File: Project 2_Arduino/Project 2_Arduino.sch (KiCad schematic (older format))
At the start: 30 parts, among them J10 Conn_01x08, J11 Conn_01x08, J12 Conn_01x06, J13 Conn_01x03, J3 USB_microB_2040002-1, J4 Conn_02x03_Odd_Even, SW1 SW_Push, U1 FT232RL, U3 ATMEGA328P-AU, Y1 16MHz

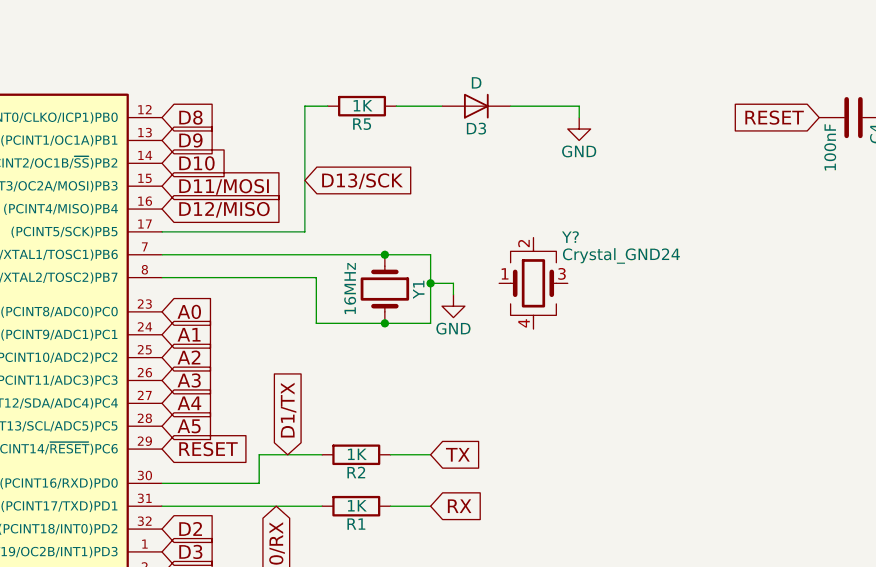
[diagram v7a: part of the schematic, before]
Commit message: new clock schematic
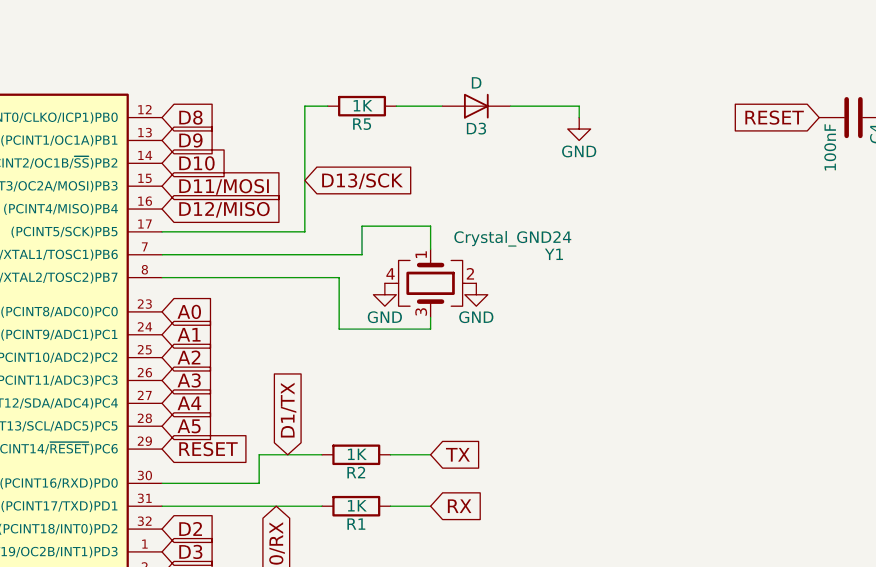
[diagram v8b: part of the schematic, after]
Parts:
- removed Y1: 16MHz, project2:TM16, symbol Crystal
- gave numbers to parts that had none: 1
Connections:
- net GND: now also Y1.2, Y1.4; no longer U3.7 ((PCINT6/XTAL1/TOSC1)PB6), U3.8 ((PCINT7/XTAL2/TOSC2)PB7)
- net at Y1.1: now also U3.7 ((PCINT6/XTAL1/TOSC1)PB6)
- net at Y1.3: now also U3.8 ((PCINT7/XTAL2/TOSC2)PB7)
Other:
- moved on the sheet: Y1
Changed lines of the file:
@@
 Text Notes 2275 1100 0    197  ~ 0
 Microcontroller
-$Comp
-L Crystal Y1
-U 1 1 59DFEE18
-P 5075 2400
-F 0 "Y1" H 5075 2550 50  0000 C CNN
-F 1 "16MHz" H 5075 2250 50  0000 C CNN
-F 2 "project2:TM16" H 5075 2400 50  0001 C CNN
-F 3 "" H 5075 2400 50  0001 C CNN
-	1    5075 2400
-	0    1    1    0
-$EndComp
 Wire Wire Line
 	2100 3950 2200 3950
@@
 Wire Wire Line
 	1200 5925 1150 5925
-Wire Wire Line
-	4100 2250 5275 2250
-Wire Wire Line
-	4100 2350 4775 2350
-Wire Wire Line
-	4775 2350 4775 2550
-Wire Wire Line
-	4775 2550 5275 2550
-Wire Wire Line
-	5275 2550 5275 2250
-Connection ~ 5075 2550
-Connection ~ 5075 2250
-Wire Wire Line
-	5275 2375 5375 2375
-Wire Wire Line
-	5375 2375 5375 2425
-Connection ~ 5275 2375
-$Comp
-L GND #PWR09
-U 1 1 59DFF36B
-P 5375 2425
-F 0 "#PWR09" H 5375 2175 50  0001 C CNN
-F 1 "GND" H 5375 2275 50  0000 C CNN
-F 2 "" H 5375 2425 50  0001 C CNN
-F 3 "" H 5375 2425 50  0001 C CNN
-	1    5375 2425
-	1    0    0    -1
-$EndComp
 Text Notes 8175 4825 0    197  ~ 0
 Header Pins
@@
 GND
 $Comp
-L Crystal_GND24 Y?
+L Crystal_GND24 Y1
 U 1 1 59DF0F95
-P 5725 2375
-F 0 "Y?" H 5850 2575 50  0000 L CNN
-F 1 "Crystal_GND24" H 5850 2500 50  0000 L CNN
-F 2 "" H 5725 2375 50  0001 C CNN
-F 3 "" H 5725 2375 50  0001 C CNN
-	1    5725 2375
-	1    0    0    -1
-$EndComp
+P 5275 2375
+F 0 "Y1" V 5150 2875 50  0000 L CNN
+F 1 "Crystal_GND24" V 5075 2475 50  0000 L CNN
+F 2 "" H 5275 2375 50  0001 C CNN
+F 3 "" H 5275 2375 50  0001 C CNN
+	1    5275 2375
+	0    1    1    0
+$EndComp
+Wire Wire Line
+	4100 2250 4975 2250
+Wire Wire Line
+	4975 2250 4975 2125
+Wire Wire Line
+	4975 2125 5275 2125
+Wire Wire Line
+	5275 2125 5275 2225
+Wire Wire Line
+	5275 2525 5275 2575
+Wire Wire Line
+	4875 2575 5275 2575
+Wire Wire Line
+	4875 2350 4875 2575
+Wire Wire Line
+	4875 2350 4100 2350
+$Comp
+L GND #PWR?
+U 1 1 59E16207
+P 5475 2375
+F 0 "#PWR?" H 5475 2125 50  0001 C CNN
+F 1 "GND" H 5475 2225 50  0000 C CNN
+F 2 "" H 5475 2375 50  0001 C CNN
+F 3 "" H 5475 2375 50  0001 C CNN
+	1    5475 2375
+	1    0    0    -1
+$EndComp
+$Comp
+L GND #PWR?
+U 1 1 59E16269
+P 5075 2375
+F 0 "#PWR?" H 5075 2125 50  0001 C CNN
+F 1 "GND" H 5075 2225 50  0000 C CNN
+F 2 "" H 5075 2375 50  0001 C CNN
+F 3 "" H 5075 2375 50  0001 C CNN
+	1    5075 2375
+	1    0    0    -1
+$EndComp
